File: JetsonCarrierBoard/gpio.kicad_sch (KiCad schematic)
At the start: 0 parts

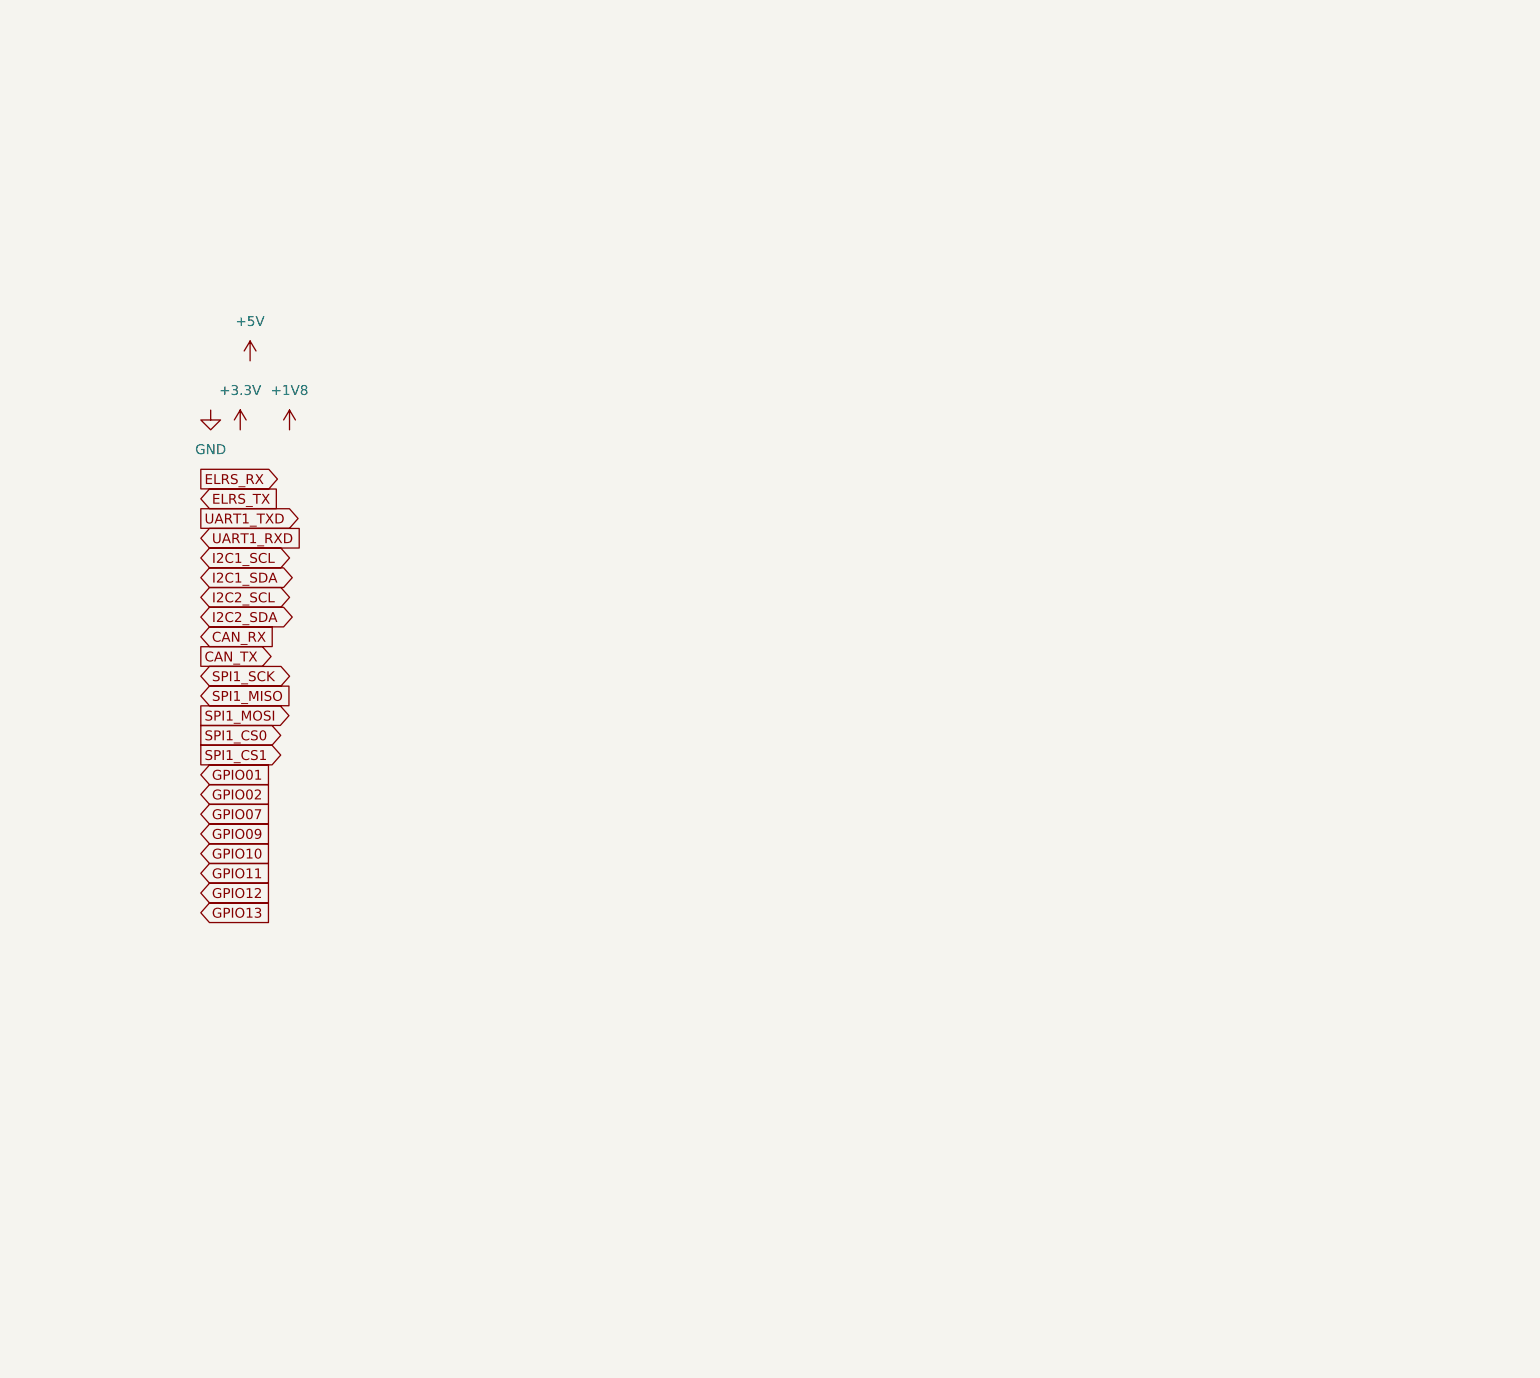
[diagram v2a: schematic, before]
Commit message: Start of GPIO header wiring
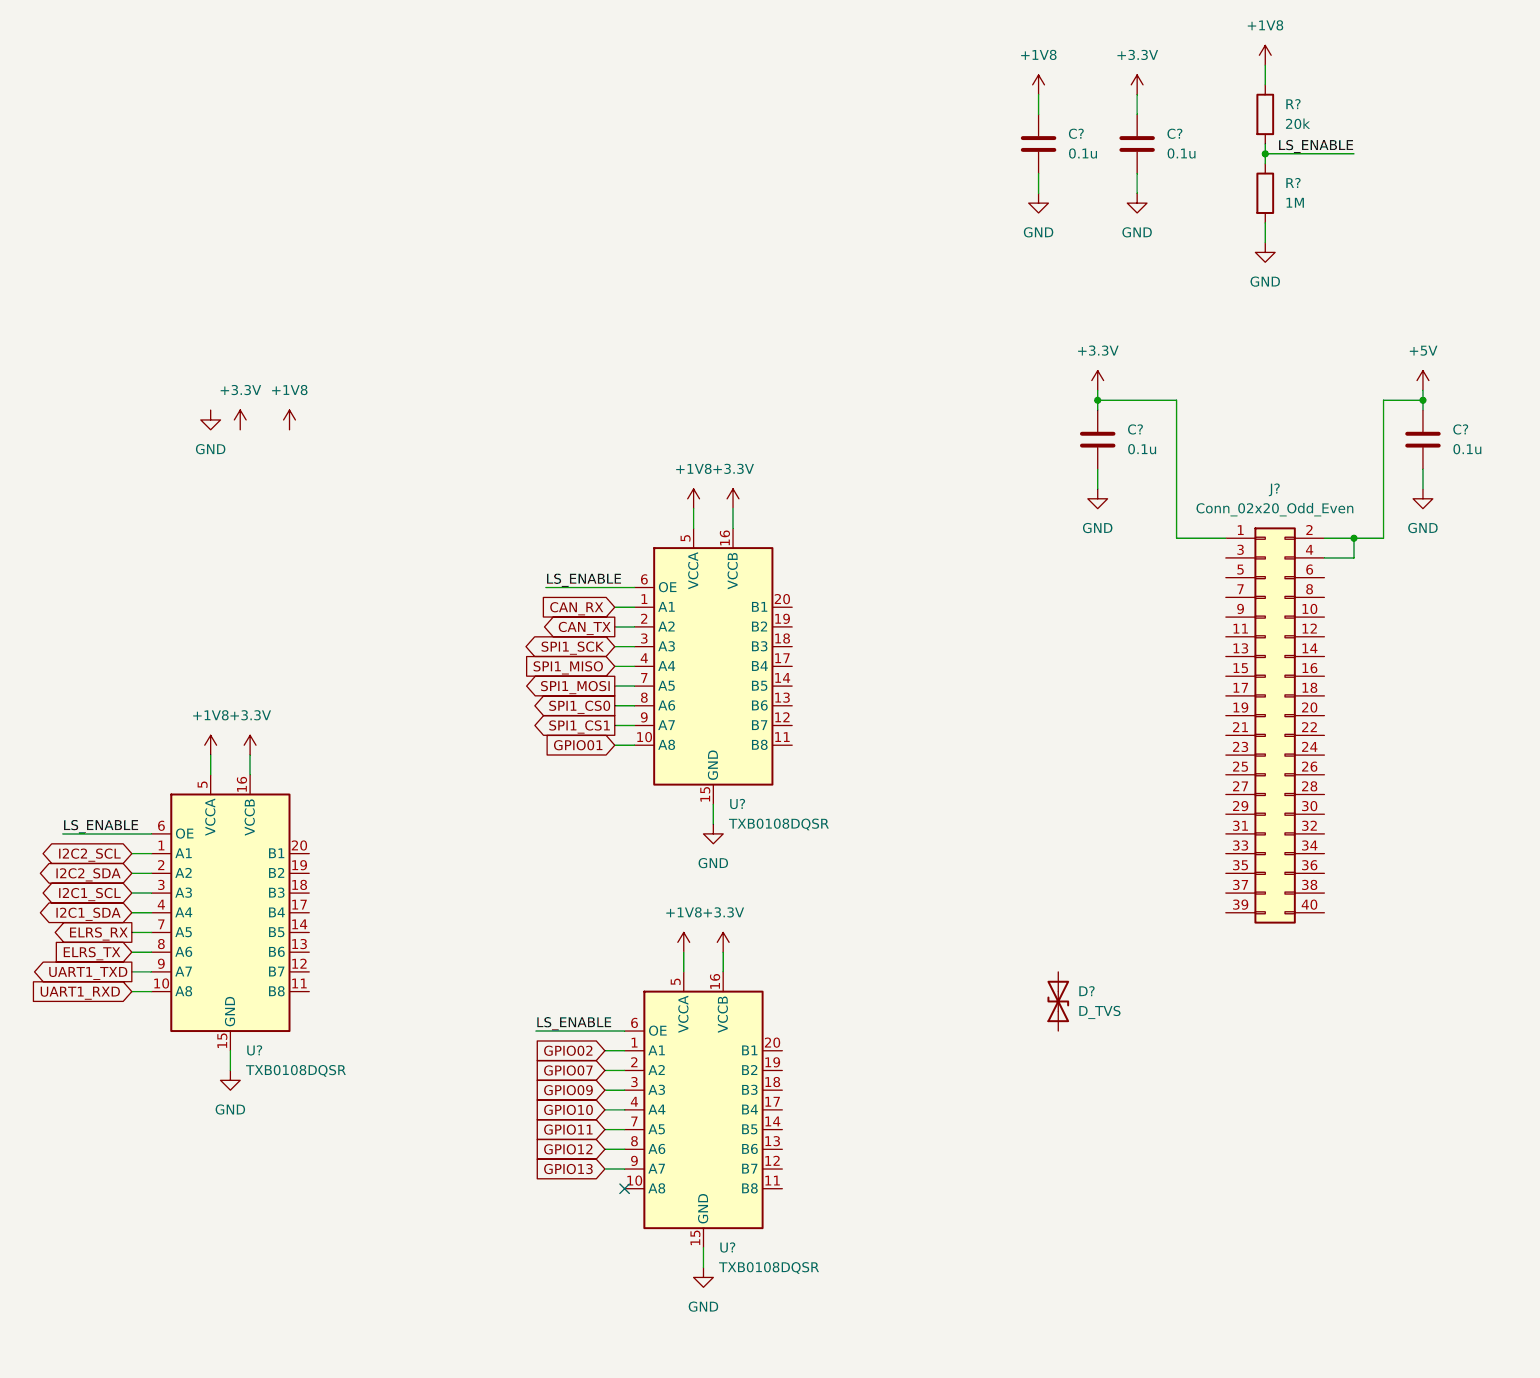
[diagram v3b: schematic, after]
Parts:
- added C? (x4): 0.1u, symbol Device:C
- added D?: D_TVS, symbol Device:D_TVS
- added J?: Conn_02x20_Odd_Even, symbol Connector_Generic:Conn_02x20_Odd_Even
- added R?: 20k, symbol Device:R
- added R?: 1M, symbol Device:R
- added U? (x3): TXB0108DQSR, Package_SON:USON-20_2x4mm_P0.4mm, symbol Logic_LevelTranslator:TXB0108DQSR
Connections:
- net +1V8: now also C?.1, R?.1, U?.5 (VCCA), U?.5 (VCCA), U?.5 (VCCA)
- net +3.3V: now also C?.1, C?.1, J?.1 (Pin_1), U?.16 (VCCB), U?.16 (VCCB), U?.16 (VCCB)
- net +5V: now also C?.1, J?.2 (Pin_2), J?.4 (Pin_4)
- net CAN_RX: now also U?.1 (A1)
- net CAN_TX: now also U?.2 (A2)
- net ELRS_RX: now also U?.7 (A5)
- net ELRS_TX: now also U?.8 (A6)
- net GND: now also C?.2, C?.2, C?.2, C?.2, R?.2, U?.15 (GND), U?.15 (GND), U?.15 (GND)
- net GPIO01: now also U?.10 (A8)
- net GPIO02: now also U?.1 (A1)
- net GPIO07: now also U?.2 (A2)
- net GPIO09: now also U?.3 (A3)
- net GPIO10: now also U?.4 (A4)
- net GPIO11: now also U?.7 (A5)
- net GPIO12: now also U?.8 (A6)
- net GPIO13: now also U?.9 (A7)
- net I2C1_SCL: now also U?.3 (A3)
- net I2C1_SDA: now also U?.4 (A4)
- net I2C2_SCL: now also U?.1 (A1)
- net I2C2_SDA: now also U?.2 (A2)
- net SPI1_CS0: now also U?.8 (A6)
- net SPI1_CS1: now also U?.9 (A7)
- net SPI1_MISO: now also U?.4 (A4)
- net SPI1_MOSI: now also U?.7 (A5)
- net SPI1_SCK: now also U?.3 (A3)
- net UART1_RXD: now also U?.10 (A8)
- net UART1_TXD: now also U?.9 (A7)
- new net LS_ENABLE: R?.1, R?.2, U?.6 (OE), U?.6 (OE), U?.6 (OE)
- no-connect marks 0 -> 1

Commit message: GPIO wiring
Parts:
- removed J?: Conn_02x20_Odd_Even, symbol Connector_Generic:Conn_02x20_Odd_Even
- removed U?: TXB0108DQSR, Package_SON:USON-20_2x4mm_P0.4mm, symbol Logic_LevelTranslator:TXB0108DQSR
- added D?: D_TVS, symbol Device:D_TVS
- added J?: (no value), symbol Connector_Generic:Conn_01x04
- added J?: (no value), symbol Connector_Generic:Conn_02x14_Odd_Even
- added Q?: (no value), symbol Transistor_FET:DMG2301L
- added R? (x4): (no value), symbol Device:R
- added U? (x2): (no value), symbol Transistor_Arrays:NST45010MW6T1G
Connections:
- net I2C2_SCL is gone; now on net GPIO07: U?.1 (A1)
- net I2C2_SDA is gone; now on net GPIO09: U?.2 (A2)
- net SPI1_CS1 is gone; now on net GPIO01: U?.9 (A7)
- net +3.3V: now also J?.1 (Pin_1), J?.13 (Pin_13), J?.4 (Pin_4), R?.2, R?.2
- net +5V: now also Q?.3 (D), U?.1 (E); no longer C?.1
- net CAN_RX: now also J?.2 (Pin_2); no longer U?.1 (A1)
- net CAN_TX: now also J?.1 (Pin_1); no longer U?.2 (A2)
- net GND: now also D?.1 (A1), D?.1 (A1), J?.15 (Pin_15), J?.16 (Pin_16), J?.22 (Pin_22), J?.23 (Pin_23), J?.3 (Pin_3), J?.6 (Pin_6), J?.7 (Pin_7), R?.2, R?.2
- net GPIO01: no longer U?.10 (A8)
- net GPIO02: now also U?.10 (A8)
- net GPIO10: now also U?.3 (A3)
- net GPIO11: now also U?.4 (A4)
- net GPIO12: now also U?.1 (A1)
- net GPIO13: now also U?.2 (A2)
- net I2C1_SCL: now also D?.2 (A2), J?.5 (Pin_5); no longer U?.3 (A3)
- net I2C1_SDA: now also D?.2 (A2), J?.3 (Pin_3); no longer U?.4 (A4)
- net UART1_RXD_LS: now reaches U?.11 (B8)
- net UART1_RXD_LS: now also J?.14 (Pin_14), R?.1
- net UART1_TXD_LS: now reaches U?.12 (B7)
- net UART1_TXD_LS: now also J?.12 (Pin_12)
- net ELRS_RX_LS: now reaches U?.13 (B6)
- net ELRS_RX_LS: now also J?.10 (Pin_10), R?.1
- net ELRS_TX_LS: now reaches U?.14 (B5)
- net ELRS_TX_LS: now also J?.8 (Pin_8)
- net GPIO11_LS: now reaches U?.17 (B4)
- net GPIO11_LS: now also J?.11 (Pin_11)
- net GPIO10_LS: now reaches U?.18 (B3)
- net GPIO10_LS: now also J?.18 (Pin_18)
- net GPIO09_LS: now reaches U?.19 (B2)
- net GPIO09_LS: now also J?.25 (Pin_25)
- net GPIO07_LS: now reaches U?.20 (B1)
- net GPIO07_LS: now also J?.9 (Pin_9)
- net GPIO01_LS: now reaches U?.11 (B8)
- net GPIO01_LS: now also J?.26 (Pin_26)
- net SPI1_CS1_LS: now reaches U?.12 (B7)
- net SPI1_CS0_LS: now reaches U?.13 (B6)
- net SPI1_CS0_LS: now also J?.20 (Pin_20)
- net SPI1_MOSI_LS: now reaches U?.14 (B5)
- net SPI1_MOSI_LS: now also J?.17 (Pin_17)
- net SPI1_MISO_LS: now reaches U?.17 (B4)
- net SPI1_MISO_LS: now also J?.19 (Pin_19)
- net SPI1_SCK_LS: now reaches U?.18 (B3)
- net SPI1_SCK_LS: now also J?.21 (Pin_21)
- net GPIO13_LS: now reaches U?.19 (B2)
- net GPIO13_LS: now also J?.27 (Pin_27)
- net GPIO12_LS: now reaches U?.20 (B1)
- net GPIO12_LS: now also J?.28 (Pin_28)
- new net: Q?.1 (G), R?.1, U?.3 (C)
- new net: R?.1, U?.2 (B), U?.5 (B), U?.6 (C)
- new net +20V: C?.1, J?.2 (Pin_2), J?.4 (Pin_4), Q?.2 (S), U?.4 (E)
- new net GPIO02_LS: J?.24 (Pin_24)
- no-connect marks 1 -> 0
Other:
- moved on the sheet: C?

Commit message: Adding more Title block info and changing main hierarchical page layout
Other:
- title: (none) -> GPIO
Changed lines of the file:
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@@
 (kicad_sch (version 20211123) (generator eeschema)
   (paper "A4")
+  (title_block
+    (title "GPIO")
+    (date "2022-09-18")
+    (rev "1.0")
+  )
   (junction (at 103.378 27.813) (diameter 0) (color 0 0 0 0)
   )
